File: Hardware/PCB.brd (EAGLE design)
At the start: 46 x 35 mm, 105 parts, among them IC1 BQ25180YBGR_BQ25180YBGR, IC2 DRV2605YZFR_DRV2605YZFR, IC3 BMA423_BMA423, IC9 RT6160AWSC_RT6160AWSC, J1 503480-2400_503480-2400, J4 KH-TYPE-C-16P, J5 TC2030-IDC_TC2030-IDC, Q3 SI1308EDL-T1-GE3, U1 NORDIC_NRF_4_NRF52840_QF, U3 MAX17048G+T10, X1 32MHz, X2 32.768kHz

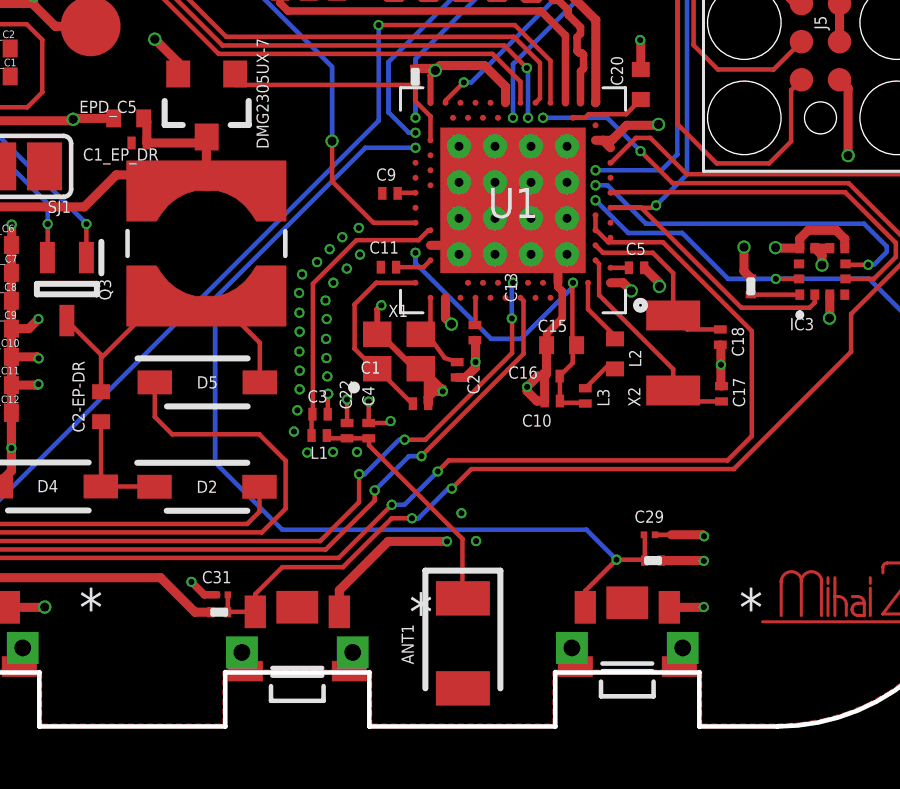
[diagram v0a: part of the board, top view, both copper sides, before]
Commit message: Fix unrouted airwires for ANT1 and U1
Signed-off-by: Mihai Zegheru <mihai.z.2005@gmail.com>
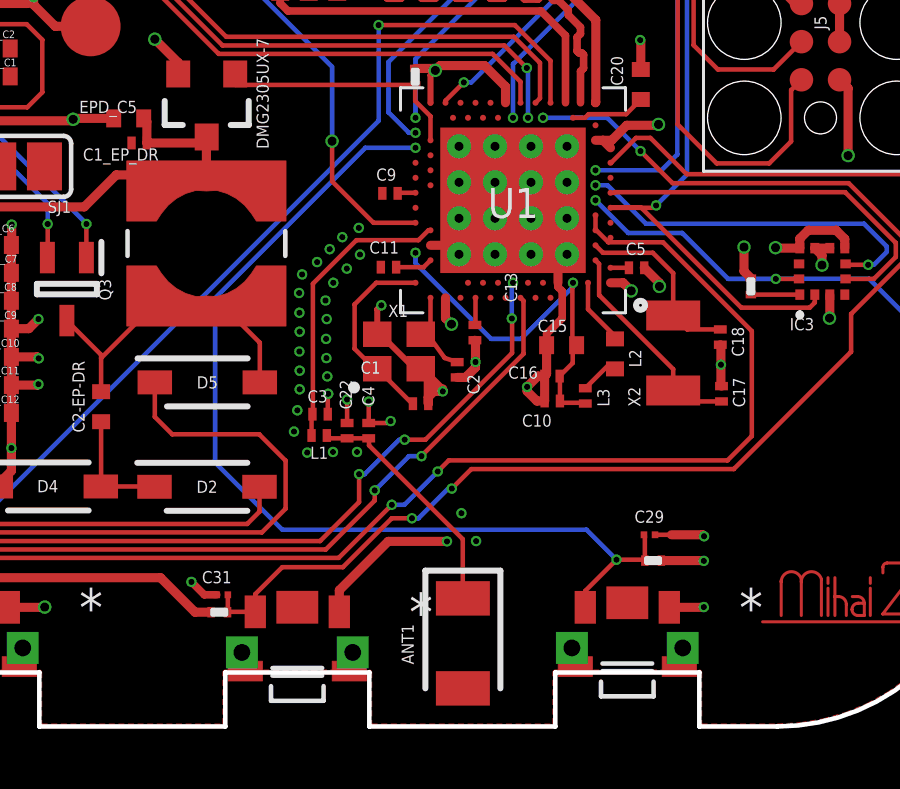
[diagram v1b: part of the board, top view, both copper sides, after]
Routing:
- net GND: track 118.2 -> 119.0 mm
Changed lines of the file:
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@@
 <layer number="14" name="Route14" color="22" fill="1" visible="no" active="no"/>
 <layer number="15" name="Route15" color="23" fill="1" visible="no" active="yes"/>
-<layer number="16" name="Bottom" color="1" fill="1" visible="yes" active="yes"/>
+<layer number="16" name="Bottom" color="1" fill="1" visible="no" active="yes"/>
 <layer number="17" name="Pads" color="2" fill="1" visible="yes" active="yes"/>
 <layer number="18" name="Vias" color="2" fill="1" visible="yes" active="yes"/>
-<layer number="19" name="Unrouted" color="6" fill="1" visible="no" active="yes"/>
+<layer number="19" name="Unrouted" color="6" fill="1" visible="yes" active="yes"/>
 <layer number="20" name="Dimension" color="24" fill="1" visible="no" active="yes"/>
 <layer number="21" name="tPlace" color="7" fill="1" visible="no" active="yes"/>
-<layer number="22" name="bPlace" color="7" fill="1" visible="yes" active="yes"/>
+<layer number="22" name="bPlace" color="7" fill="1" visible="no" active="yes"/>
 <layer number="23" name="tOrigins" color="15" fill="1" visible="yes" active="yes"/>
 <layer number="24" name="bOrigins" color="15" fill="1" visible="yes" active="yes"/>
-<layer number="25" name="tNames" color="7" fill="1" visible="yes" active="yes"/>
+<layer number="25" name="tNames" color="7" fill="1" visible="no" active="yes"/>
 <layer number="26" name="bNames" color="7" fill="1" visible="no" active="yes"/>
 <layer number="27" name="tValues" color="7" fill="1" visible="no" active="yes"/>
 <layer number="28" name="bValues" color="7" fill="1" visible="no" active="yes"/>
-<layer number="29" name="tStop" color="7" fill="3" visible="yes" active="yes"/>
-<layer number="30" name="bStop" color="7" fill="6" visible="yes" active="yes"/>
-<layer number="31" name="tCream" color="7" fill="4" visible="yes" active="yes"/>
-<layer number="32" name="bCream" color="7" fill="5" visible="yes" active="yes"/>
-<layer number="33" name="tFinish" color="6" fill="3" visible="yes" active="yes"/>
-<layer number="34" name="bFinish" color="6" fill="6" visible="yes" active="yes"/>
-<layer number="35" name="tGlue" color="7" fill="4" visible="yes" active="yes"/>
-<layer number="36" name="bGlue" color="7" fill="5" visible="yes" active="yes"/>
+<layer number="29" name="tStop" color="7" fill="3" visible="no" active="yes"/>
+<layer number="30" name="bStop" color="7" fill="6" visible="no" active="yes"/>
+<layer number="31" name="tCream" color="7" fill="4" visible="no" active="yes"/>
+<layer number="32" name="bCream" color="7" fill="5" visible="no" active="yes"/>
+<layer number="33" name="tFinish" color="6" fill="3" visible="no" active="yes"/>
+<layer number="34" name="bFinish" color="6" fill="6" visible="no" active="yes"/>
+<layer number="35" name="tGlue" color="7" fill="4" visible="no" active="yes"/>
+<layer number="36" name="bGlue" color="7" fill="5" visible="no" active="yes"/>
 <layer number="37" name="tTest" color="7" fill="1" visible="no" active="yes"/>
 <layer number="38" name="bTest" color="7" fill="1" visible="no" active="yes"/>
@@
 <layer number="47" name="Measures" color="7" fill="1" visible="no" active="yes"/>
 <layer number="48" name="Document" color="7" fill="1" visible="no" active="yes"/>
-<layer number="49" name="Reference" color="7" fill="1" visible="yes" active="yes"/>
+<layer number="49" name="Reference" color="7" fill="1" visible="no" active="yes"/>
 <layer number="50" name="dxf" color="7" fill="1" visible="no" active="no"/>
-<layer number="51" name="tDocu" color="7" fill="1" visible="yes" active="yes"/>
+<layer number="51" name="tDocu" color="7" fill="1" visible="no" active="yes"/>
 <layer number="52" name="bDocu" color="7" fill="1" visible="no" active="yes"/>
 <layer number="53" name="tGND_GNDA" color="7" fill="1" visible="no" active="no"/>
@@
 <wire x1="1.08" y1="-7.895" x2="0.985" y2="-7.8" width="0.1524" layer="1"/>
 <wire x1="1.66" y1="-7.895" x2="2.38" y2="-7.895" width="0.1524" layer="1"/>
-<wire x1="5.21" y1="-13.23" x2="5.52" y2="-13.23" width="0.1524" layer="1"/>
-<wire x1="5.505" y1="-13.525" x2="5.21" y2="-13.23" width="0.1524" layer="1"/>
-<wire x1="4.835" y1="-12.855" x2="4.81" y2="-12.83" width="0.1524" layer="1"/>
 <wire x1="2.38" y1="-7.895" x2="2.39" y2="-7.905" width="0.1524" layer="1"/>
 <wire x1="2.39" y1="-7.905" x2="2.39" y2="-8.13" width="0.1524" layer="1"/>
-<wire x1="2.39" y1="-8.13" x2="5.505" y2="-11.245" width="0.1524" layer="1"/>
-<wire x1="5.505" y1="-11.245" x2="5.505" y2="-13.525" width="0.1524" layer="1"/>
-<wire x1="5.52" y1="-13.23" x2="4.835" y2="-12.855" width="0" layer="19" extent="1-1"/>
+<wire x1="2.39" y1="-8.13" x2="5.515" y2="-11.255" width="0.1524" layer="1"/>
+<wire x1="5.515" y1="-11.255" x2="5.515" y2="-13.225" width="0.1524" layer="1"/>
+<wire x1="5.515" y1="-13.225" x2="5.52" y2="-13.23" width="0.1524" layer="1"/>
+<wire x1="5.52" y1="-13.23" x2="5.21" y2="-13.23" width="0.1524" layer="1"/>
+<wire x1="5.21" y1="-13.23" x2="4.81" y2="-12.83" width="0.1524" layer="1"/>
 </signal>
 <signal name="N$7">
@@
 <wire x1="20.835" y1="-13.885" x2="20.71" y2="-14.01" width="0.1016" layer="1" curve="-90"/>
 <wire x1="20.71" y1="-14.01" x2="15.51" y2="-14.01" width="0.1016" layer="1"/>
+<wire x1="7.19" y1="0.04" x2="7.79" y2="0.64" width="0.1524" layer="1"/>
 <wire x1="17.69" y1="-13.8" x2="17.92" y2="-13.8" width="0" layer="19" extent="1-1"/>
 <wire x1="17.69" y1="-12.73" x2="17.69" y2="-12.89" width="0" layer="19" extent="1-1"/>
@@
 <wire x1="19.52" y1="-12.38" x2="19.1" y2="-12.54" width="0" layer="19" extent="1-1"/>
 <wire x1="13.55" y1="-13.52" x2="15.51" y2="-14.01" width="0" layer="19" extent="1-1"/>
-<wire x1="7.19" y1="0.04" x2="6.59" y2="0.64" width="0" layer="19" extent="1-1"/>
 </signal>
 <signal name="N$10">
